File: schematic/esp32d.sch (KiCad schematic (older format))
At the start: 47 parts, among them IC1 CP2102N-A01-GQFN28R, J1 USB_B_Micro, J2 Conn_02x08_Odd_Even, J3 Conn_02x08_Odd_Even, J4 Conn_01x02, Q1 SS8050-G, Q2 SS8050-G, Q3 DMG2307L-7, SW1 SW_Push, U1 AMS1117-3.3, U2 ESP32-WROOM-32D, U3 DizzyBITLogo, U4 MCP73831-2-OT

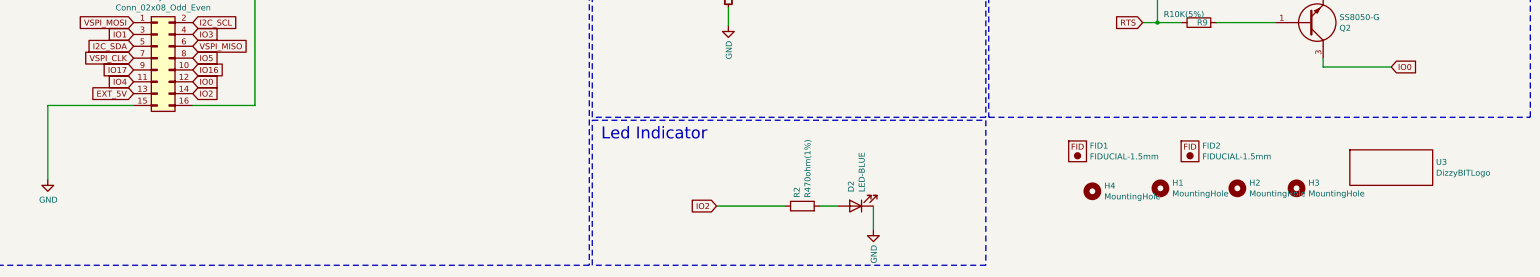
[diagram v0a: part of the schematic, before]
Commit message: Added Standard module design
Added Part numbers
Modified footprint positions to match standard module design
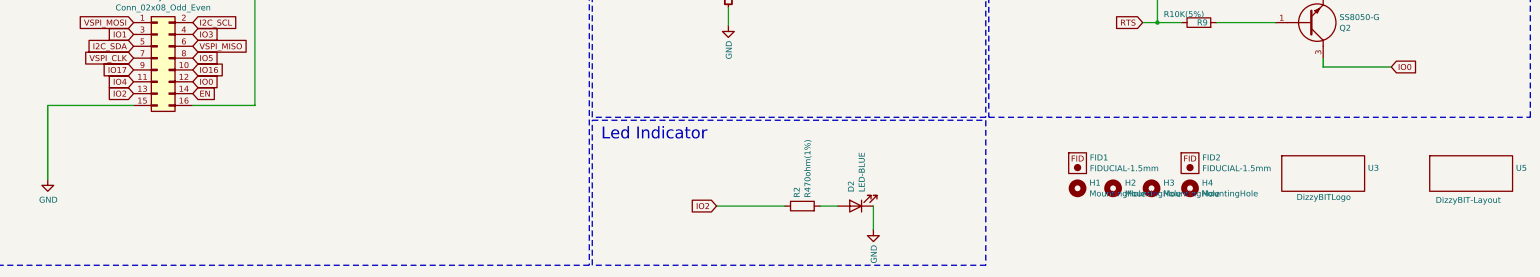
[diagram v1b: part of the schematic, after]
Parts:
- added U5: DizzyBIT-Layout, DizzyBit:DizzyBit-Din Rail Module, symbol undo:DizzyBITLogo
- D6: dk_pn (none) -> 475-2560-1-ND; dk_web (none) -> https://www.digikey.com/product-detail/en/osram-opto-semico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; pn (none) -> LY R976-PS-36
- J2, J3: pn (none) -> PC104-003-2*8-B-1
- J4: pn (none) -> DS1066-06-2-M-R-B-1-R
- Q3: dk_pn (none) -> DMG2307L-7DITR-ND; dk_web (none) -> https://www.digikey.com/product-detail/en/diodes-incorporat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; pn (none) -> DMG2307L-7
- R10: footprint Capacitor_SMD:C_0603_1608Metric -> Resistor_SMD:R_0805_2012Metric; pn (none) -> 0805W8F1001T5E
- U4: dk_pn (none) -> MCP73831T-2ATI/OTCT-ND; dk_web (none) -> https://www.digikey.com/product-detail/en/microchip-technol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; pn (none) -> MCP73831T-2ATI/OT
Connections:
- net EN: now also J3.14 (Pin_14)
- net EXT_5V: no longer J3.13 (Pin_13)
- net IO2: now also J3.13 (Pin_13); no longer J3.14 (Pin_14)
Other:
- moved on the sheet: FID1, FID2, H1, H2, H3, H4, U3
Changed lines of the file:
@@
 F 1 "Conn_02x08_Odd_Even" H 4350 7901 50  0000 C CNN
 F 2 "Connector_PinHeader_2.54mm:PinHeader_2x08_P2.54mm_Vertical" H 4300 7475 50  0001 C CNN
-F 3 "~" H 4300 7475 50  0001 C CNN
+F 3 "http://www.connfly.com/userfiles/image/UpLoadFile/File/2014/11/24/PC104-003.pdf" H 4300 7475 50  0001 C CNN
+F 4 "PC104-003-2*8-B-1" H 4300 7475 50  0001 C CNN "pn"
 	1    4300 7475
-	1    0    0    -1
-$EndComp
-$Comp
-L Connector_Generic:Conn_02x08_Odd_Even J3
-U 1 1 5D8B5A40
-P 4325 9300
-F 0 "J3" H 4375 9817 50  0000 C CNN
-F 1 "Conn_02x08_Odd_Even" H 4375 9726 50  0000 C CNN
-F 2 "Connector_PinHeader_2.54mm:PinHeader_2x08_P2.54mm_Vertical" H 4325 9300 50  0001 C CNN
-F 3 "~" H 4325 9300 50  0001 C CNN
-	1    4325 9300
 	1    0    0    -1
 $EndComp
@@
 Text GLabel 4125 9100 0    50   Input ~ 0
 IO1
-Text GLabel 4625 9600 2    50   Input ~ 0
+Text GLabel 4125 9600 0    50   Input ~ 0
 IO2
 Text GLabel 4625 9100 2    50   Input ~ 0
@@
 I39
 Text GLabel 4600 7775 2    50   Input ~ 0
-EXT_5V
-Text GLabel 4125 9600 0    50   Input ~ 0
 EXT_5V
 Text GLabel 2575 2900 0    50   Input ~ 0
@@
 L Mechanical:MountingHole H4
 U 1 1 5C8FAF19
-P 12225 10425
-F 0 "H4" H 12325 10471 50  0000 L CNN
-F 1 "MountingHole" H 12325 10380 50  0000 L CNN
-F 2 "MountingHole:MountingHole_2.2mm_M2_DIN965_Pad" H 12225 10425 50  0001 C CNN
-F 3 "~" H 12225 10425 50  0001 C CNN
-	1    12225 10425
+P 13050 10400
+F 0 "H4" H 13150 10446 50  0000 L CNN
+F 1 "MountingHole" H 13150 10355 50  0000 L CNN
+F 2 "MountingHole:MountingHole_2.2mm_M2_DIN965_Pad" H 13050 10400 50  0001 C CNN
+F 3 "~" H 13050 10400 50  0001 C CNN
+	1    13050 10400
 	1    0    0    -1
 $EndComp
@@
 L Mechanical:MountingHole H1
 U 1 1 5C902F86
-P 12800 10400
-F 0 "H1" H 12900 10446 50  0000 L CNN
-F 1 "MountingHole" H 12900 10355 50  0000 L CNN
-F 2 "MountingHole:MountingHole_2.2mm_M2_DIN965_Pad" H 12800 10400 50  0001 C CNN
-F 3 "~" H 12800 10400 50  0001 C CNN
-	1    12800 10400
+P 12100 10400
+F 0 "H1" H 12200 10446 50  0000 L CNN
+F 1 "MountingHole" H 12200 10355 50  0000 L CNN
+F 2 "MountingHole:MountingHole_2.2mm_M2_DIN965_Pad" H 12100 10400 50  0001 C CNN
+F 3 "~" H 12100 10400 50  0001 C CNN
+	1    12100 10400
 	1    0    0    -1
 $EndComp
@@
 L Mechanical:MountingHole H2
 U 1 1 5C902FE8
-P 13450 10400
-F 0 "H2" H 13550 10446 50  0000 L CNN
-F 1 "MountingHole" H 13550 10355 50  0000 L CNN
-F 2 "MountingHole:MountingHole_2.2mm_M2_DIN965_Pad" H 13450 10400 50  0001 C CNN
-F 3 "~" H 13450 10400 50  0001 C CNN
-	1    13450 10400
+P 12400 10400
+F 0 "H2" H 12500 10446 50  0000 L CNN
+F 1 "MountingHole" H 12500 10355 50  0000 L CNN
+F 2 "MountingHole:MountingHole_2.2mm_M2_DIN965_Pad" H 12400 10400 50  0001 C CNN
+F 3 "~" H 12400 10400 50  0001 C CNN
+	1    12400 10400
 	1    0    0    -1
 $EndComp
@@
 L Mechanical:MountingHole H3
 U 1 1 5C90304E
-P 13950 10400
-F 0 "H3" H 14050 10446 50  0000 L CNN
-F 1 "MountingHole" H 14050 10355 50  0000 L CNN
-F 2 "MountingHole:MountingHole_2.2mm_M2_DIN965_Pad" H 13950 10400 50  0001 C CNN
-F 3 "~" H 13950 10400 50  0001 C CNN
-	1    13950 10400
+P 12725 10400
+F 0 "H3" H 12825 10446 50  0000 L CNN
+F 1 "MountingHole" H 12825 10355 50  0000 L CNN
+F 2 "MountingHole:MountingHole_2.2mm_M2_DIN965_Pad" H 12725 10400 50  0001 C CNN
+F 3 "~" H 12725 10400 50  0001 C CNN
+	1    12725 10400
 	1    0    0    -1
 $EndComp
@@
 L undo:DizzyBITLogo U3
 U 1 1 5C903A70
-P 14750 10225
-F 0 "U3" H 15128 10271 50  0000 L CNN
-F 1 "DizzyBITLogo" H 15128 10180 50  0000 L CNN
-F 2 "undo:DizzyBIT_silk_20" H 14750 10225 50  0001 C CNN
-F 3 "" H 14750 10225 50  0001 C CNN
-	1    14750 10225
+P 14175 10275
+F 0 "U3" H 14553 10321 50  0000 L CNN
+F 1 "DizzyBITLogo" H 13950 10075 50  0000 L CNN
+F 2 "undo:DizzyBIT_silk_20" H 14175 10275 50  0001 C CNN
+F 3 "" H 14175 10275 50  0001 C CNN
+	1    14175 10275
 	1    0    0    -1
 $EndComp
@@
 L pcb:FIDUCIAL-1.5mm FID1
 U 1 1 5D240B4A
-P 12100 10100
-F 0 "FID1" H 12203 10159 50  0000 L CNN
-F 1 "FIDUCIAL-1.5mm" H 12203 10068 50  0000 L CNN
-F 2 "fab:FIDUCIAL-1.5mm" H 12100 9900 60  0001 C CNN
-F 3 "" H 12100 10075 60  0000 C CNN
-	1    12100 10100
+P 12100 10200
+F 0 "FID1" H 12203 10259 50  0000 L CNN
+F 1 "FIDUCIAL-1.5mm" H 12203 10168 50  0000 L CNN
+F 2 "fab:FIDUCIAL-1.5mm" H 12100 10000 60  0001 C CNN
+F 3 "" H 12100 10175 60  0000 C CNN
+	1    12100 10200
 	1    0    0    -1
 $EndComp
@@
 L pcb:FIDUCIAL-1.5mm FID2
 U 1 1 5D240BD6
-P 13050 10100
-F 0 "FID2" H 13153 10159 50  0000 L CNN
-F 1 "FIDUCIAL-1.5mm" H 13153 10068 50  0000 L CNN
-F 2 "fab:FIDUCIAL-1.5mm" H 13050 9900 60  0001 C CNN
-F 3 "" H 13050 10075 60  0000 C CNN
-	1    13050 10100
+P 13050 10200
+F 0 "FID2" H 13153 10259 50  0000 L CNN
+F 1 "FIDUCIAL-1.5mm" H 13153 10168 50  0000 L CNN
+F 2 "fab:FIDUCIAL-1.5mm" H 13050 10000 60  0001 C CNN
+F 3 "" H 13050 10175 60  0000 C CNN
+	1    13050 10200
 	1    0    0    -1
 $EndComp
@@
 F 2 "Package_TO_SOT_SMD:SOT-23" H 13925 1400 50  0001 L CNN
 F 3 "https://componentsearchengine.com/Datasheets/1/DMG2307L-7.pdf" H 13925 1300 50  0001 L CNN
-F 4 "P-Channel Enhancement MOSFET SOT-23 Diodes Inc DMG2307L-7 P-channel MOSFET Transistor, -2 A, -30 V, 3-Pin SOT23" H 13925 1200 50  0001 L CNN "Description"
-F 5 "1.1" H 13925 1100 50  0001 L CNN "Height"
-F 6 "621-DMG2307L-7" H 13925 1000 50  0001 L CNN "Mouser Part Number"
-F 7 "https://www.mouser.com/Search/Refine.aspx?Keyword=621-DMG2307L-7" H 13925 900 50  0001 L CNN "Mouser Price/Stock"
-F 8 "Diodes Inc." H 13925 800 50  0001 L CNN "Manufacturer_Name"
-F 9 "DMG2307L-7" H 13925 700 50  0001 L CNN "Manufacturer_Part_Number"
+F 4 "DMG2307L-7DITR-ND" H 13475 1450 50  0001 C CNN "dk_pn"
+F 5 "DMG2307L-7" H 13475 1450 50  0001 C CNN "pn"
+F 6 "https://www.digikey.com/product-detail/en/diodes-incorporated/DMG2307L-7/DMG2307L-7DITR-ND/2756043" H 13475 1450 50  0001 C CNN "dk_web"
+F 7 "P-Channel Enhancement MOSFET SOT-23 Diodes Inc DMG2307L-7 P-channel MOSFET Transistor, -2 A, -30 V, 3-Pin SOT23" H 13925 1200 50  0001 L CNN "Description"
+F 8 "1.1" H 13925 1100 50  0001 L CNN "Height"
+F 9 "621-DMG2307L-7" H 13925 1000 50  0001 L CNN "Mouser Part Number"
+F 10 "https://www.mouser.com/Search/Refine.aspx?Keyword=621-DMG2307L-7" H 13925 900 50  0001 L CNN "Mouser Price/Stock"
+F 11 "Diodes Inc." H 13925 800 50  0001 L CNN "Manufacturer_Name"
+F 12 "DMG2307L-7" H 13925 700 50  0001 L CNN "Manufacturer_Part_Number"
 	1    13475 1450
 	1    0    0    -1
@@
 F 2 "Package_TO_SOT_SMD:SOT-23-5" H 9575 5700 50  0001 L CIN
 F 3 "http://ww1.microchip.com/downloads/en/DeviceDoc/20001984g.pdf" H 9375 5900 50  0001 C CNN
+F 4 "MCP73831T-2ATI/OTCT-ND" H 9525 5950 50  0001 C CNN "dk_pn"
+F 5 "MCP73831T-2ATI/OT" H 9525 5950 50  0001 C CNN "pn"
+F 6 "https://www.digikey.com/product-detail/en/microchip-technology/MCP73831T-2ATI-OT/MCP73831T-2ATI-OTCT-ND/1979803" H 9525 5950 50  0001 C CNN "dk_web"
 	1    9525 5950
 	0    -1   -1   0
@@
 F 1 "Conn_01x02" H 8195 5491 50  0000 C CNN
 F 2 "Connector_JST:JST_PH_S2B-PH-SM4-TB_1x02-1MP_P2.00mm_Horizontal" H 8275 5725 50  0001 C CNN
-F 3 "~" H 8275 5725 50  0001 C CNN
+F 3 "http://www.connfly.com/userfiles/image/UpLoadFile/File/2017/8/30/DS1066-06.pdf" H 8275 5725 50  0001 C CNN
+F 4 "DS1066-06-2-M-R-B-1-R" H 8275 5725 50  0001 C CNN "pn"
 	1    8275 5725
 	-1   0    0    1
@@
 F 1 "LED-YELLOW" H 10125 5450 50  0000 R CNN
 F 2 "LED_SMD:LED_0805_2012Metric" H 9900 5350 50  0001 C CNN
-F 3 "" H 9900 5350 50  0001 C CNN
+F 3 "https://dammedia.osram.info/media/resource/hires/osram-dam-2492854/LY%20R976.pdf" H 9900 5350 50  0001 C CNN
+F 4 "475-2560-1-ND" H 9900 5350 50  0001 C CNN "dk_pn"
+F 5 "LY R976-PS-36" H 9900 5350 50  0001 C CNN "pn"
+F 6 "https://www.digikey.com/product-detail/en/osram-opto-semiconductors-inc/LY-R976-PS-36/475-2560-1-ND/1802687" H 9900 5350 50  0001 C CNN "dk_web"
 	1    9900 5350
 	1    0    0    1
@@
 F 0 "R10" V 9993 5350 50  0000 C CNN
 F 1 "R1K" V 10084 5350 50  0000 C CNN
-F 2 "Capacitor_SMD:C_0603_1608Metric" V 10130 5350 50  0001 C CNN
+F 2 "Resistor_SMD:R_0805_2012Metric" V 10130 5350 50  0001 C CNN
 F 3 "" H 10200 5350 50  0001 C CNN
+F 4 "0805W8F1001T5E " H 10200 5350 50  0001 C CNN "pn"
 	1    10200 5350
 	0    -1   -1   0
@@
 	1    0    0    -1
 $EndComp
+Text GLabel 4625 9600 2    50   Input ~ 0
+EN
+$Comp
+L undo:DizzyBITLogo U5
+U 1 1 5D8F1399
+P 15425 10275
+F 0 "U5" H 15803 10321 50  0000 L CNN
+F 1 "DizzyBIT-Layout" H 15125 10050 50  0000 L CNN
+F 2 "DizzyBit:DizzyBit-Din Rail Module" H 15425 10275 50  0001 C CNN
+F 3 "" H 15425 10275 50  0001 C CNN
+	1    15425 10275
+	1    0    0    -1
+$EndComp
+$Comp
+L Connector_Generic:Conn_02x08_Odd_Even J3
+U 1 1 5D8FF691
+P 4325 9300
+F 0 "J3" H 4375 9817 50  0000 C CNN
+F 1 "Conn_02x08_Odd_Even" H 4375 9726 50  0000 C CNN
+F 2 "Connector_PinHeader_2.54mm:PinHeader_2x08_P2.54mm_Vertical" H 4325 9300 50  0001 C CNN
+F 3 "http://www.connfly.com/userfiles/image/UpLoadFile/File/2014/11/24/PC104-003.pdf" H 4325 9300 50  0001 C CNN
+F 4 "PC104-003-2*8-B-1" H 4325 9300 50  0001 C CNN "pn"
+	1    4325 9300
+	1    0    0    -1
+$EndComp

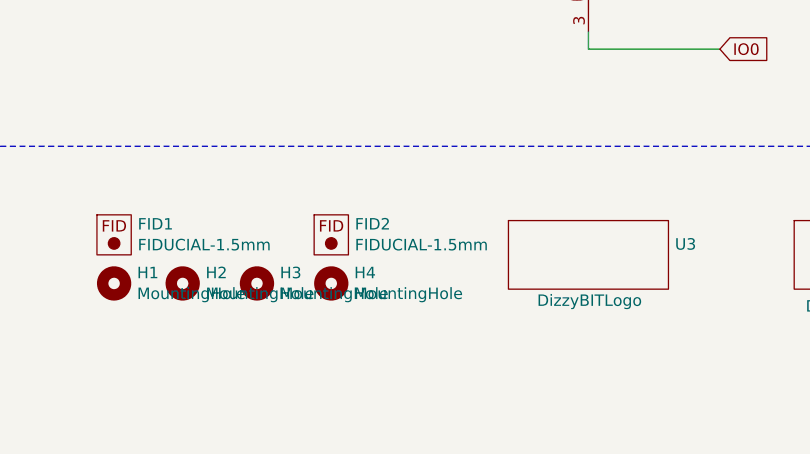
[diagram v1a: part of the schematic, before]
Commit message: Repositioned LEDs to match the standard module design
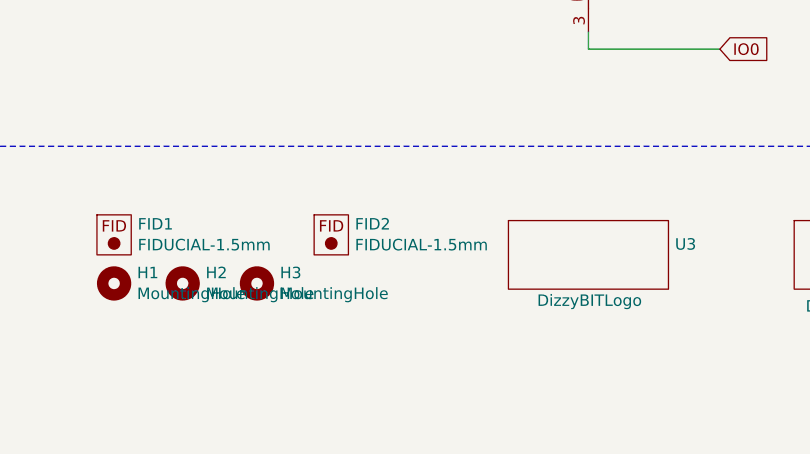
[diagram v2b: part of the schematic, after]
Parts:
- removed H4: MountingHole, MountingHole:MountingHole_2.2mm_M2_DIN965_Pad, symbol Mechanical:MountingHole
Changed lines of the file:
@@
 EESchema Schematic File Version 4
+LIBS:esp32d-cache
 EELAYER 26 0
 EELAYER END
@@
 	1    0    0    -1
 $EndComp
-$Comp
-L Mechanical:MountingHole H4
-U 1 1 5C8FAF19
-P 13050 10400
-F 0 "H4" H 13150 10446 50  0000 L CNN
-F 1 "MountingHole" H 13150 10355 50  0000 L CNN
-F 2 "MountingHole:MountingHole_2.2mm_M2_DIN965_Pad" H 13050 10400 50  0001 C CNN
-F 3 "~" H 13050 10400 50  0001 C CNN
-	1    13050 10400
-	1    0    0    -1
-$EndComp

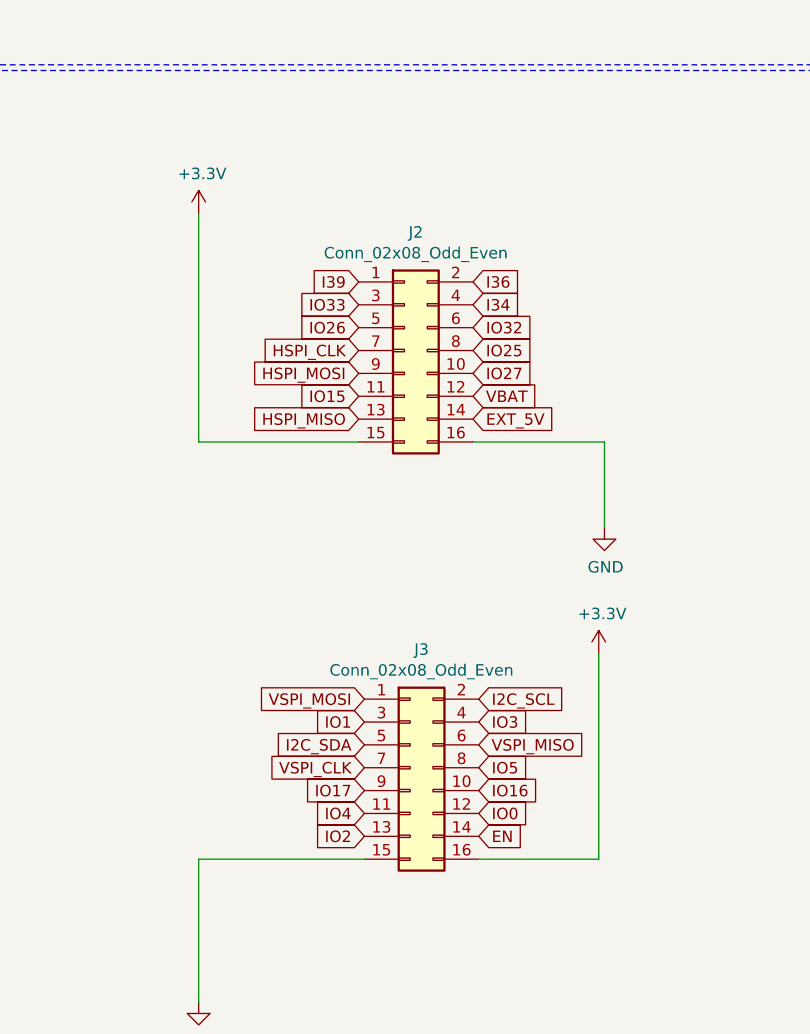
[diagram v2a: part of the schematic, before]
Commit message: Changed 3.3V position for better PCB exposure
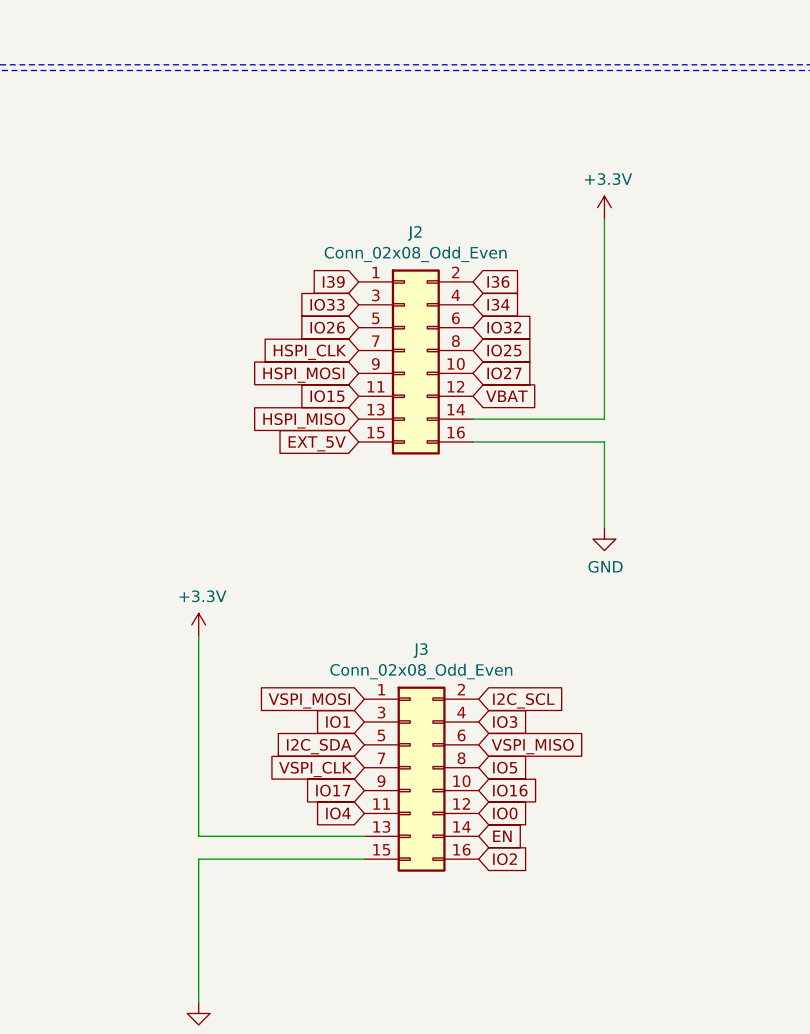
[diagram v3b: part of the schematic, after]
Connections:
- net +3V3: now also J2.14 (Pin_14), J3.13 (Pin_13); no longer J2.15 (Pin_15), J3.16 (Pin_16)
- net EXT_5V: now also J2.15 (Pin_15); no longer J2.14 (Pin_14)
- net IO2: now also J3.16 (Pin_16); no longer J3.13 (Pin_13)
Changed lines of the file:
@@
 L power:+3.3V #PWR0101
 U 1 1 5D8B5B52
-P 3400 6875
-F 0 "#PWR0101" H 3400 6725 50  0001 C CNN
-F 1 "+3.3V" H 3415 7048 50  0000 C CNN
-F 2 "" H 3400 6875 50  0001 C CNN
-F 3 "" H 3400 6875 50  0001 C CNN
-	1    3400 6875
-	1    0    0    -1
-$EndComp
-Wire Wire Line
-	3400 7875 4100 7875
+P 5175 6900
+F 0 "#PWR0101" H 5175 6750 50  0001 C CNN
+F 1 "+3.3V" H 5190 7073 50  0000 C CNN
+F 2 "" H 5175 6900 50  0001 C CNN
+F 3 "" H 5175 6900 50  0001 C CNN
+	1    5175 6900
+	1    0    0    -1
+$EndComp
 $Comp
 L power:GND #PWR0102
@@
 L power:+3.3V #PWR0103
 U 1 1 5D8B5BF6
-P 5150 8800
-F 0 "#PWR0103" H 5150 8650 50  0001 C CNN
-F 1 "+3.3V" H 5165 8973 50  0000 C CNN
-F 2 "" H 5150 8800 50  0001 C CNN
-F 3 "" H 5150 8800 50  0001 C CNN
-	1    5150 8800
+P 3400 8725
+F 0 "#PWR0103" H 3400 8575 50  0001 C CNN
+F 1 "+3.3V" H 3415 8898 50  0000 C CNN
+F 2 "" H 3400 8725 50  0001 C CNN
+F 3 "" H 3400 8725 50  0001 C CNN
+	1    3400 8725
 	1    0    0    -1
 $EndComp
@@
 $EndComp
 Wire Wire Line
-	4625 9700 5150 9700
-Wire Wire Line
-	5150 9700 5150 8800
-Wire Wire Line
 	5175 8250 5175 7875
-Wire Wire Line
-	3400 7875 3400 6875
 Text GLabel 4125 9200 0    50   Input ~ 0
 I2C_SDA
@@
 Text GLabel 4125 9100 0    50   Input ~ 0
 IO1
-Text GLabel 4125 9600 0    50   Input ~ 0
+Text GLabel 4625 9700 2    50   Input ~ 0
 IO2
 Text GLabel 4625 9100 2    50   Input ~ 0
@@
 Text GLabel 4100 7175 0    50   Input ~ 0
 I39
-Text GLabel 4600 7775 2    50   Input ~ 0
+Text GLabel 4100 7875 0    50   Input ~ 0
 EXT_5V
 Text GLabel 2575 2900 0    50   Input ~ 0
@@
 	1    0    0    -1
 $EndComp
+Wire Wire Line
+	4600 7775 5175 7775
+Wire Wire Line
+	5175 7775 5175 6900
+Wire Wire Line
+	4125 9600 3400 9600
+Wire Wire Line
+	3400 9600 3400 8725
 $EndSCHEMATC

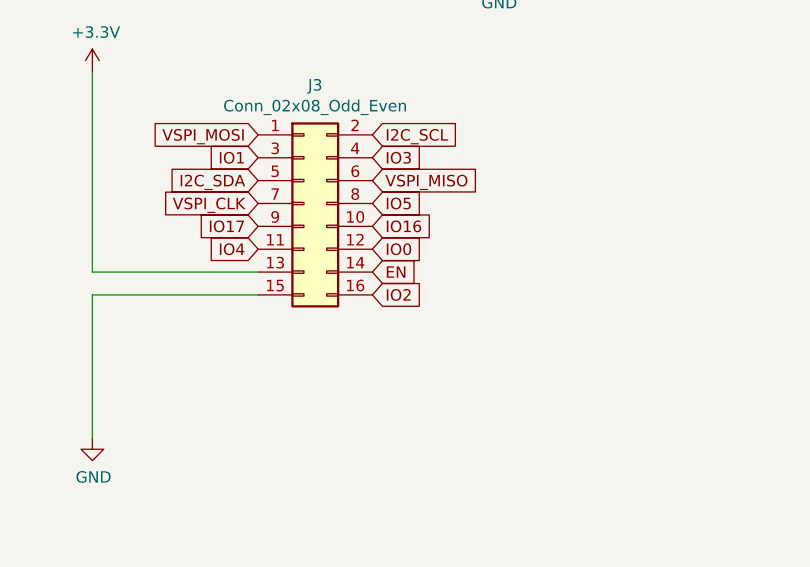
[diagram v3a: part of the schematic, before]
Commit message: Changed EN and IO2 position
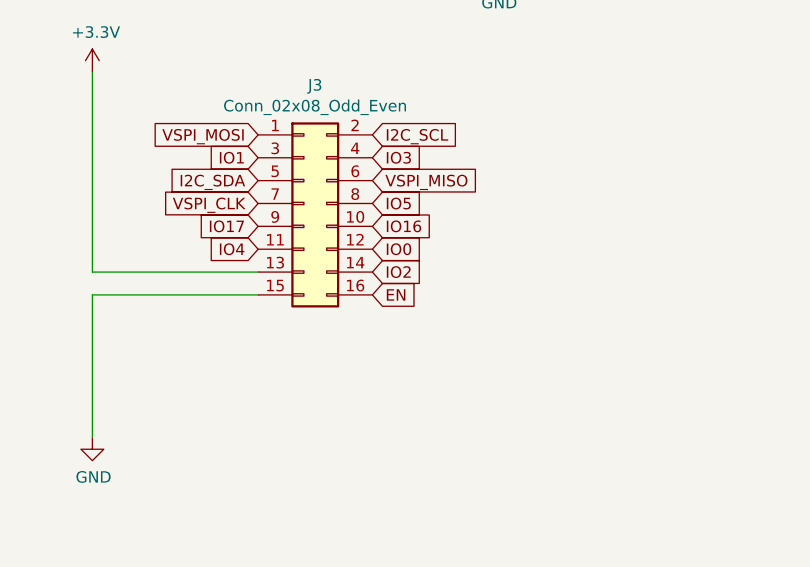
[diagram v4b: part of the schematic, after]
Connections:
- net EN: now also J3.16 (Pin_16); no longer J3.14 (Pin_14)
- net IO2: now also J3.14 (Pin_14); no longer J3.16 (Pin_16)
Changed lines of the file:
@@
 Text GLabel 4125 9100 0    50   Input ~ 0
 IO1
-Text GLabel 4625 9700 2    50   Input ~ 0
+Text GLabel 4625 9600 2    50   Input ~ 0
 IO2
 Text GLabel 4625 9100 2    50   Input ~ 0
@@
 	1    0    0    -1
 $EndComp
-Text GLabel 4625 9600 2    50   Input ~ 0
+Text GLabel 4625 9700 2    50   Input ~ 0
 EN
 $Comp
